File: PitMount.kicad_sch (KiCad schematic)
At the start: 12 parts, among them J1 Conn_01x08_Pin, Q3 AO3400A, U1 UnifyNano, U2 ELRS-Rx

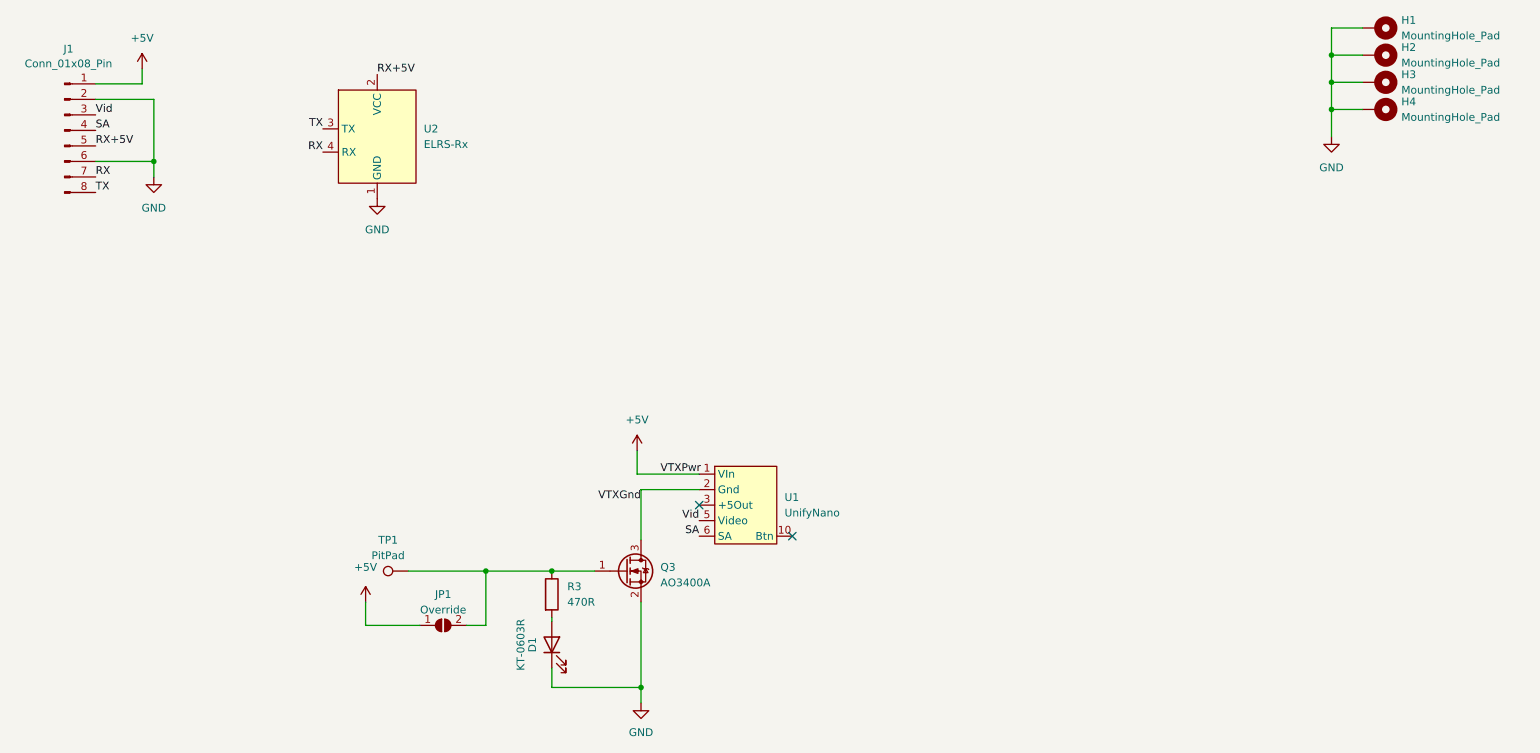
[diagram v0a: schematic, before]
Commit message: Update schematic with npn bjt and p-channel mosfet
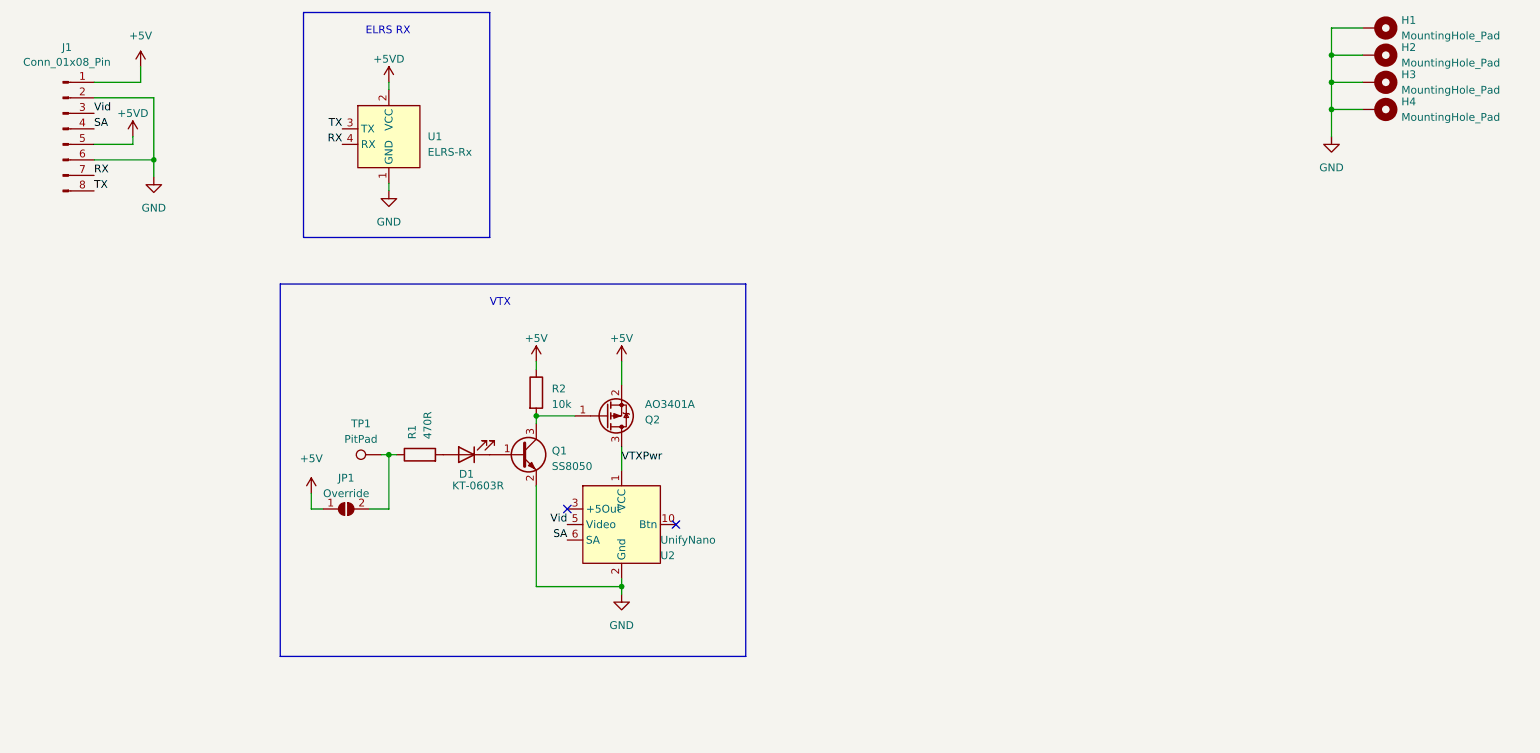
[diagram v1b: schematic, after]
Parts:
- removed Q3: AO3400A, Package_TO_SOT_SMD:SOT-23, symbol Transistor_FET:AO3400A
- added Q1: SS8050, Package_TO_SOT_SMD:SOT-23, symbol Transistor_BJT:BC817
- added Q2: AO3401A, Package_TO_SOT_SMD:SOT-23, symbol Transistor_FET:AO3401A
- added R2: 10k, Resistor_SMD:R_0402_1005Metric, symbol Device:R
- renumbered R3 to R1, U2 to U1, U1 to U2
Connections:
- net VTXGnd is gone; now on net GND: U2.2 (Gnd), U2.4 (Gnd), U2.7 (Gnd), U2.8 (Gnd), U2.9 (Gnd)
- net +5V: now also Q2.2 (S), R2.1; no longer U2.1 (VIn)
- net GND: now also Q1.2 (E); no longer D1.1 (K)
- net RX+5V renamed +5VD
- new net: Q1.3 (C), Q2.1 (G), R2.2
- new net: D1.1 (K), Q1.1 (B)
- new net VTXPwr: Q2.3 (D), U2.1 (VCC)
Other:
- note added: "ELRS RX"
- note added: "VTX"
- moved on the sheet: D1, JP1, R1, TP1, U1, U2
